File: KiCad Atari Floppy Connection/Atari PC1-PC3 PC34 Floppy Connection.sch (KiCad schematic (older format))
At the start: 2 parts, among them J1 Atari PC1-PC3 external floppy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, J2 PC34 Floppy Cable

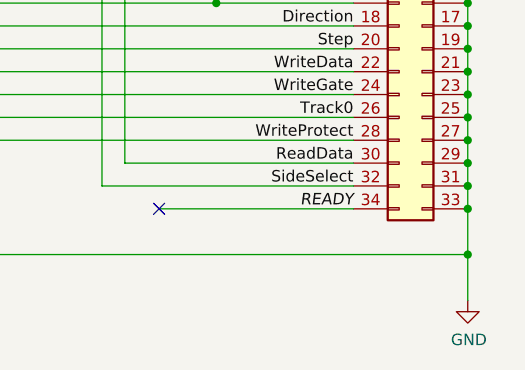
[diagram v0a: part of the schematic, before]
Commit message: PWR_FLAG to GND
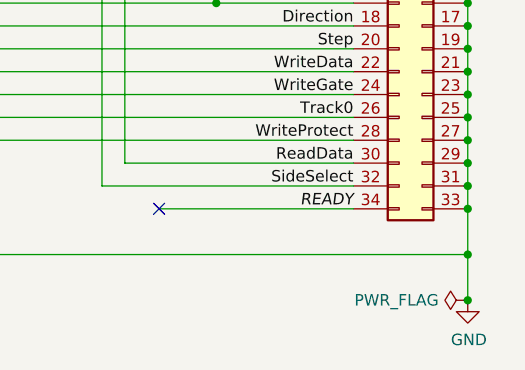
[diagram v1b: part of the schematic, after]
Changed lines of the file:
@@
 Wire Wire Line
 	3300 3200 5350 3200
-Connection ~ 5350 3200
-Wire Wire Line
-	5350 3200 5350 3400
 Text Label 4850 2100 2    50   ~ 0
 MotorOn2
@@
 Wire Wire Line
 	2600 2100 4250 2100
+Wire Wire Line
+	5350 3400 5350 3200
+Connection ~ 5350 3200
+$Comp
+L power:PWR_FLAG #FLG0101
+U 1 1 610AE458
+P 5350 3400
+F 0 "#FLG0101" H 5350 3475 50  0001 C CNN
+F 1 "PWR_FLAG" V 5350 3527 50  0000 L CNN
+F 2 "" H 5350 3400 50  0001 C CNN
+F 3 "~" H 5350 3400 50  0001 C CNN
+	1    5350 3400
+	0    -1   -1   0
+$EndComp
+Connection ~ 5350 3400
 $EndSCHEMATC
